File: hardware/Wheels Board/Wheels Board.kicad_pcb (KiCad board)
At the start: 2 copper layers, 45 parts, among them J1 53307-2471, J2 MX150_02x04_Vertical, J4 Conn_01x08_Socket, U1 XIAO-ESP32-S3-SMD, U2 ASM330LHHTR, U4 TPS5405DR, U5 TLV9002QDRQ1

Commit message: added uart to sch
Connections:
- J1 pad 17: /IMU_SPI_CLK -> /IMU_SPI_MOSI
- J1 pad 4: /IMU_SPI_CLK -> /ESP_UART_RX
- J1 pad 6: /IMU_SPI_CLK -> /ESP_UART_TX
- J4 pad 7: /IMU_SPI_CLK -> /IMU_SPI_MOSI
- U1 pad 3: unconnected-(U1-GPIO3_A2_D2-Pad3) -> /XIAO_HEARTBEAT_LED
- U1 pad 7: /XIAO_HEARTBEAT_LED -> /ESP_UART_TX
- U1 pad 8: unconnected-(U1-GPIO44_D7_RX-Pad8) -> /ESP_UART_RX
- U2 pad 14: /IMU_SPI_CLK -> /IMU_SPI_MOSI
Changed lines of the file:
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@@
 	(net 53 "unconnected-(U1-GPIO5_A4_D4_SDA-Pad5)")
 	(net 54 "unconnected-(U1-MTCK-Pad22)")
-	(net 55 "unconnected-(U1-GPIO3_A2_D2-Pad3)")
+	(net 55 "/ESP_UART_TX")
 	(net 56 "unconnected-(U1-MTMS-Pad21)")
 	(net 57 "unconnected-(U1-MTDO-Pad18)")
@@
 	(net 62 "unconnected-(U1-3V3-Pad12)")
 	(net 63 "unconnected-(U1-GPIO6_A5_D5_SCL-Pad6)")
-	(net 64 "unconnected-(U1-GPIO44_D7_RX-Pad8)")
+	(net 64 "/ESP_UART_RX")
 	(net 65 "unconnected-(U2-NC-Pad10)")
 	(net 66 "unconnected-(U2-NC-Pad11)")
@@
 	(net 69 "unconnected-(U5-IN2--Pad3)")
 	(net 70 "/HALL_FEEDBACK")
+	(net 71 "/IMU_SPI_MOSI")
 	(footprint "ASM330LHHTR-IMU:LGA-14L_2P5X3X0P83_STM"
 		(layer "F.Cu")
@@
 			(size 0.351536 0.57658)
 			(layers "F.Cu" "F.Mask" "F.Paste")
-			(net 19 "/IMU_SPI_CLK")
+			(net 71 "/IMU_SPI_MOSI")
 			(pinfunction "SDA")
 			(pintype "input")
@@
 			(size 0.55 1.8)
 			(layers "F.Cu" "F.Mask" "F.Paste")
-			(net 19 "/IMU_SPI_CLK")
+			(net 64 "/ESP_UART_RX")
 			(pinfunction "I2C1_SDA")
 			(pintype "bidirectional")
@@
 			(size 0.55 1.8)
 			(layers "F.Cu" "F.Mask" "F.Paste")
-			(net 19 "/IMU_SPI_CLK")
+			(net 55 "/ESP_UART_TX")
 			(pinfunction "I2C1_SCL")
 			(pintype "output")
@@
 			(size 0.55 1.8)
 			(layers "F.Cu" "F.Mask" "F.Paste")
-			(net 19 "/IMU_SPI_CLK")
+			(net 71 "/IMU_SPI_MOSI")
 			(pinfunction "SPI1_MOSI")
 			(pintype "output")
@@
 			(layers "*.Cu" "*.Mask")
 			(remove_unused_layers no)
-			(net 19 "/IMU_SPI_CLK")
+			(net 71 "/IMU_SPI_MOSI")
 			(pinfunction "Pin_7")
 			(pintype "passive")
@@
 			(layers "F.Cu" "F.Mask" "F.Paste")
 			(roundrect_rratio 0.25)
-			(net 55 "unconnected-(U1-GPIO3_A2_D2-Pad3)")
+			(net 15 "/XIAO_HEARTBEAT_LED")
 			(pinfunction "GPIO3_A2_D2")
-			(pintype "passive+no_connect")
+			(pintype "passive")
 			(solder_mask_margin 0.0508)
 			(thermal_bridge_angle 45)
@@
 			(layers "F.Cu" "F.Mask" "F.Paste")
 			(roundrect_rratio 0.25)
-			(net 15 "/XIAO_HEARTBEAT_LED")
+			(net 55 "/ESP_UART_TX")
 			(pinfunction "GPIO43_A6_D6_TX")
 			(pintype "passive")
@@
 			(layers "F.Cu" "F.Mask" "F.Paste")
 			(roundrect_rratio 0.25)
-			(net 64 "unconnected-(U1-GPIO44_D7_RX-Pad8)")
+			(net 64 "/ESP_UART_RX")
 			(pinfunction "GPIO44_D7_RX")
-			(pintype "passive+no_connect")
+			(pintype "passive")
 			(solder_mask_margin 0.0508)
 			(thermal_bridge_angle 45)

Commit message: concepts of revA layout
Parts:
- removed J2: MX150_02x04_Vertical, UTSVT_Connectors:CONN_SD-75757-002_2X04_F16p09_MOL
- removed R10, R11: 10k, Resistor_SMD:R_0603_1608Metric_Pad0.98x0.95mm_HandSolder
- removed R12, R13: 0, Resistor_SMD:R_0603_1608Metric_Pad0.98x0.95mm_HandSolder
- added J3: Conn_02x04_Counter_Clockwise, Connector_PinHeader_2.54mm:PinHeader_2x04_P2.54mm_Vertical, F.Cu at (130.5, 107.6)
- J4: value Conn_01x08_Socket -> 757571121; footprint Connector_PinHeader_2.54mm:PinHeader_1x08_P2.54mm_Vertical -> mx150_2x2:CONN_SD-75757-002_2X02_F11p20_MOL; moved to B.Cu
- TP_3.3, TP_5V1, TP_GND1: moved to B.Cu
- moved U2 49.1 mm to (128.8, 71.8)
- moved TP_5V1 48.8 mm to (89.2, 69.8), turned to 180 degrees
- moved HALL_PWR1 48.3 mm to (80.8, 107.8)
- moved TP_3.3 48.1 mm to (89.2, 66.8), turned to 180 degrees
- moved C2 47.4 mm to (131.4, 68.4), turned to 90 degrees
- moved TP_GND1 46.6 mm to (89.2, 63.8), turned to 180 degrees
- moved C3 44.7 mm to (125.4, 71.6), turned to 90 degrees
- moved C1 41.8 mm to (128.6, 68.8), turned to 180 degrees
- moved HALL_OUT1 41.6 mm to (87.0, 107.8)
- moved D2 40.6 mm to (80.6, 85.6), turned to 180 degrees
- moved D1 38.5 mm to (80.6, 84.0), turned to 180 degrees
- moved L2 37.9 mm to (120.0, 104.4)
- moved HALL_GND1 37.4 mm to (92.0, 108.0)
- moved D3 36.8 mm to (80.6, 82.4), turned to 180 degrees
- moved D4 30.5 mm to (80.6, 87.1), turned to 180 degrees
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- renumbered TP_GND2 to HALL_GND1, TP_OUT1 to HALL_OUT1, TP_5V2 to HALL_PWR1
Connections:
- J4 pad 1: /ESP_SPI_SS -> +24V
- J4 pad 2: /ESP_SPI_CLK -> /CAN_H
- J4 pad 3: /ESP_SPI_MOSI -> /CAN_L
- J4 pad 4: /ESP_SPI_MISO -> GND
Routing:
- net +3.3V: track 0.00 -> 122.2 mm, vias 0 -> 10
- net +5V: track 0.00 -> 115.5 mm, vias 0 -> 4
- net +24V: track 0.00 -> 83.4 mm, vias 0 -> 5
- net /ESP_SPI_CLK: track 0.00 -> 78.1 mm, vias 0 -> 4
- net /HALL_OUT: track 0.00 -> 75.1 mm, vias 0 -> 6
- net /ESP_SPI_MOSI: track 0.00 -> 70.7 mm, vias 0 -> 4
- net /ESP_SPI_MISO: track 0.00 -> 70.7 mm, vias 0 -> 3
- net Net-(D6-K): track 0.00 -> 69.4 mm, vias 0 -> 2
- net /ESP_SPI_SS: track 0.00 -> 54.2 mm, vias 0 -> 3
- net /IMU_SPI_MOSI: track 0.00 -> 44.4 mm, vias 0 -> 4
- net /IMU_SPI_MISO: track 0.00 -> 43.1 mm, vias 0 -> 2
- net /IMU_SPI_CLK: track 0.00 -> 42.6 mm, vias 0 -> 5
- net /ESP_UART_RX: track 0.00 -> 39.4 mm
- net /XIAO_HEARTBEAT_LED: track 0.00 -> 39.0 mm, vias 0 -> 2
- net /EXTRA_GPIO1: track 0.00 -> 38.1 mm, vias 0 -> 6
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- added copper zone on F.Cu, net GND
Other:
- board outline added: 53.7 x 50.4 mm

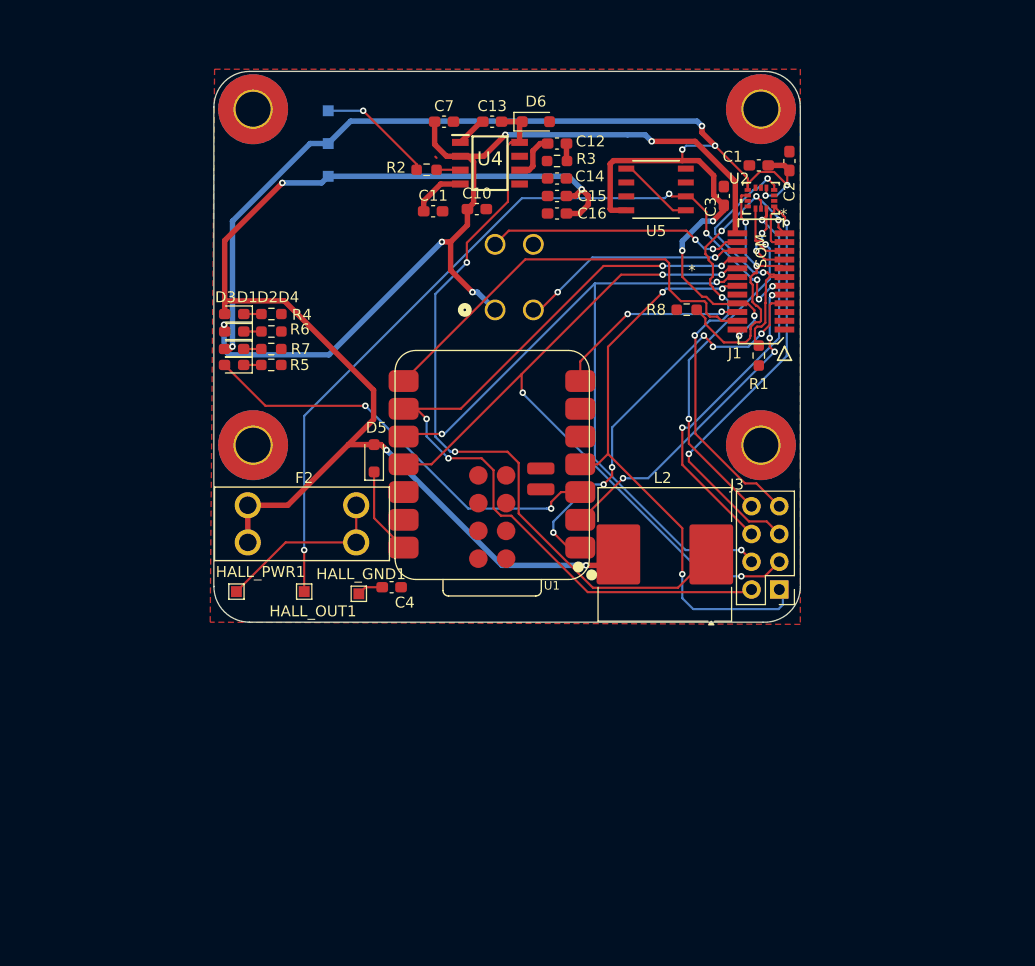
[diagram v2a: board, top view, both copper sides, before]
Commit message: review council changes, layout not finalized
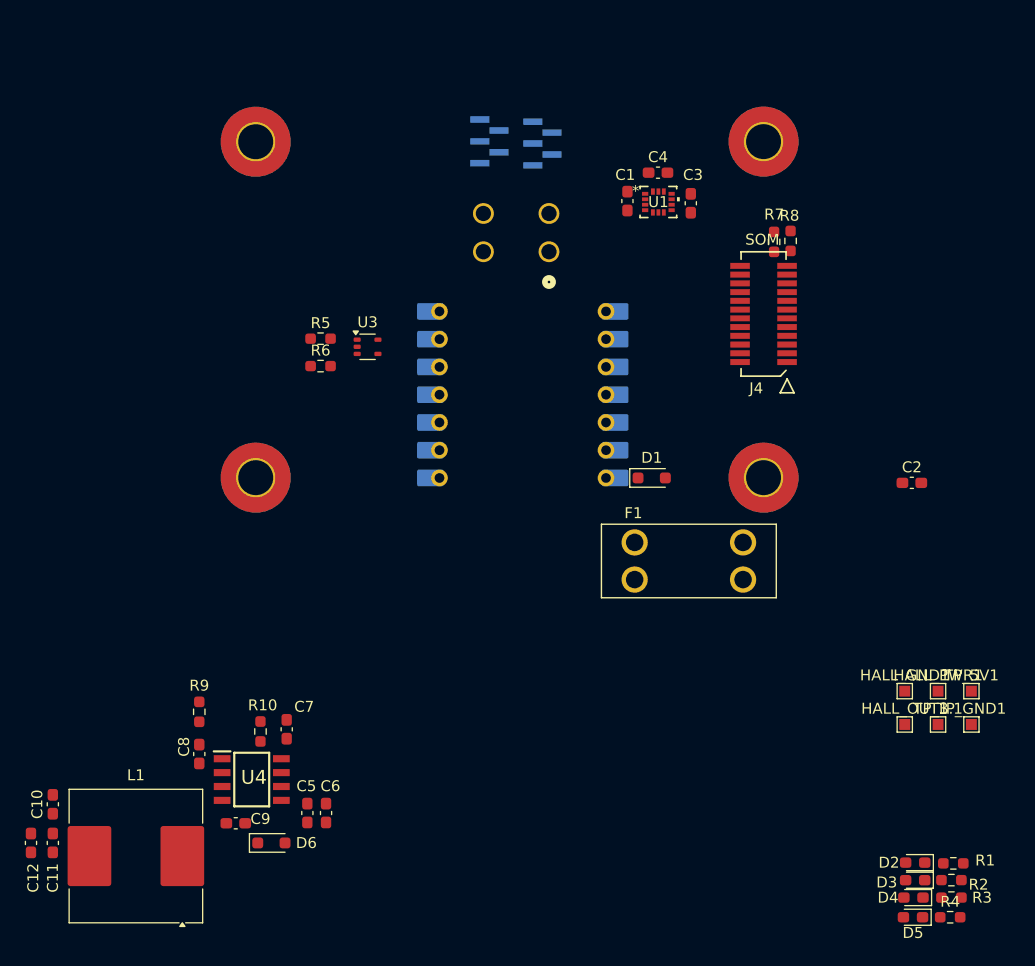
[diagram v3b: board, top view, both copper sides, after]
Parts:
- removed C13: 0.1uF, Capacitor_SMD:C_0603_1608Metric_Pad1.08x0.95mm_HandSolder
- removed C14, C15, C16: 10uF, Capacitor_SMD:C_0603_1608Metric_Pad1.08x0.95mm_HandSolder
- removed F2: Fuse, Fuse:FUSE_3568
- removed L2: 100uH, Inductor_SMD:L_Coilcraft_MSS1246-XXX
- removed TP_3.3: TestPoint, TestPoint:TestPoint_Pad_1.0x1.0mm
- removed U5: TLV9002QDRQ1, TLV9002QDRQ1:SOIC8_D_TEX
- added C5: 10uF, Capacitor_SMD:C_0603_1608Metric_Pad1.08x0.95mm_HandSolder, F.Cu at (87.3, 128.1)
- added C6: 1uF, Capacitor_SMD:C_0603_1608Metric_Pad1.08x0.95mm_HandSolder, F.Cu at (89.0, 128.1)
- added C8: 3.3nF, Capacitor_SMD:C_0603_1608Metric_Pad1.08x0.95mm_HandSolder, F.Cu at (77.4, 122.7)
- added C9: 0.1uF, Capacitor_SMD:C_0603_1608Metric_Pad1.08x0.95mm_HandSolder, F.Cu at (80.7, 129.0)
- added F1: Fuse, Fuse:FUSE_3568, F.Cu at (122.2, 105.0)
- added J2: Conn_01x05, Connector_PinHeader_1.00mm:PinHeader_1x05_P1.00mm_Vertical_SMD_Pin1Left, B.Cu at (108.8, 66.8)
- added L1: 100uH, Inductor_SMD:L_Coilcraft_MSS1246-XXX, F.Cu at (71.6, 132.0)
- added R10: ROSC, Resistor_SMD:R_0603_1608Metric_Pad0.98x0.95mm_HandSolder, F.Cu at (83.0, 120.6)
- added R9: 16k, Resistor_SMD:R_0603_1608Metric_Pad0.98x0.95mm_HandSolder, F.Cu at (77.4, 118.8)
- added TP_3.1: TestPoint, TestPoint:TestPoint_Pad_1.0x1.0mm, F.Cu at (145.0, 120.0)
- added U3: TLV9001IDCK, Package_TO_SOT_SMD:SOT-353_SC-70-5, F.Cu at (92.8, 85.4)
- C1: value 10uf -> 100nf
- C10: value 1uF -> 10uF
- C11: value 10nF -> 10uF
- C12: value 3.3nF -> 10uF
- C3: value 100nf -> 10uf
- C7: value 10uF -> 10nF
- D1: value LED -> MBR0520; footprint LED_SMD:LED_0603_1608Metric_Pad1.05x0.95mm_HandSolder -> Diode_SMD:D_SOD-323_HandSoldering
- D5: value MBR0520 -> LED; footprint Diode_SMD:D_SOD-323_HandSoldering -> LED_SMD:LED_0603_1608Metric_Pad1.05x0.95mm_HandSolder
- J1: value 53307-2471 -> Conn_01x05; footprint UTSVT_Connectors:PeripheralSOM -> Connector_PinHeader_1.00mm:PinHeader_1x05_P1.00mm_Vertical_SMD_Pin1Left; moved to B.Cu
- J3: value Conn_02x04_Counter_Clockwise -> Conn_01x04; footprint Connector_PinHeader_2.54mm:PinHeader_2x04_P2.54mm_Vertical -> mx150_2x2:CONN_SD-75757-002_2X02_F11p20_MOL; moved to B.Cu
- J4: value 757571121 -> 53307-2471; footprint mx150_2x2:CONN_SD-75757-002_2X02_F11p20_MOL -> UTSVT_Connectors:PeripheralSOM; moved to F.Cu
- R1: value 10k -> 1.5k
- R2: value ROSC -> 1.5k
- R3: value 16k -> 1.5k
- R5, R7: value 1.5k -> 10k
- R6: value 1.5k -> 19k
- TP_5V1, TP_GND1: moved to F.Cu
- U1: value XIAO-ESP32-S3-SMD -> ASM330LHHTR; footprint XIAO-ESP32S3-SMD:XIAO-ESP32S3-SMD -> ASM330LHHTR-IMU:LGA-14L_2P5X3X0P83_STM
- U2: value ASM330LHHTR -> XIAO-ESP32-S3-SMD; footprint ASM330LHHTR-IMU:LGA-14L_2P5X3X0P83_STM -> XIAO-ESP32S3:XIAO-ESP32S3-DIP; moved to B.Cu
- moved R4 83.1 mm to (146.1, 137.6)
- moved TP_GND1 81.3 mm to (148.1, 120.0), turned to 0 degrees
- moved D3 81.0 mm to (142.9, 134.2)
- moved R2 80.8 mm to (146.2, 134.2), turned to 0 degrees
- moved C12 80.1 mm to (62.0, 130.8), turned to 90 degrees
- moved D4 79.0 mm to (142.8, 135.8)
- moved D2 78.1 mm to (142.9, 132.6)
- moved R3 76.5 mm to (146.2, 135.8), turned to 0 degrees
- moved TP_5V1 75.4 mm to (148.1, 116.9), turned to 0 degrees
- moved D6 70.3 mm to (84.0, 130.8)
- moved C11 67.5 mm to (64.0, 130.8), turned to 90 degrees
- moved C10 66.9 mm to (64.0, 127.3), turned to 90 degrees
- moved HALL_PWR1 64.8 mm to (145.0, 116.9)
- moved D5 64.8 mm to (142.7, 137.6), turned to 180 degrees
- moved U4 60.5 mm to (82.2, 125.0)
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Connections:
- C10 pad 1: +24V -> +5V
- C11 pad 1: Net-(U4-SS) -> +5V
- C12 pad 1: Net-(U4-COMP) -> +5V
- C12 pad 2: Net-(C12-Pad2) -> GND
- C2 pad 1: +3.3V -> Net-(C2-Pad1)
- C4 pad 1: Net-(C4-Pad1) -> +3.3V
- C7 pad 1: +24V -> Net-(U4-SS)
- D1 pad 2: +24V -> +5V
- D2 pad 2: +3.3V -> +5V
- D3 pad 2: +5V -> +24V
- D4 pad 2: /XIAO_HEARTBEAT_LED -> +3.3V
- D5 pad 2: +5V -> /XIAO_HEARTBEAT_LED
- HALL_GND1 pad 1: Net-(C4-Pad1) -> GND
- HALL_PWR1 pad 1: Net-(F2-Pad2) -> Net-(C2-Pad1)
- J1 pad 1: GND -> /ESP_SPI_SS
- J1 pad 2: +3.3V -> /ESP_SPI_CLK
- J1 pad 3: GND -> /ESP_SPI_MOSI
- J1 pad 4: /ESP_UART_RX -> /ESP_SPI_MISO
- J3 pad 1: /ESP_SPI_SS -> +24V
- J3 pad 2: /ESP_SPI_CLK -> /CAN_H
- J3 pad 3: /ESP_SPI_MOSI -> /CAN_L
- J3 pad 4: /ESP_SPI_MISO -> GND
- J4 pad 1: +24V -> GND
- J4 pad 2: /CAN_H -> +3.3V
- J4 pad 3: /CAN_L -> GND
- J4 pad 4: GND -> /ESP_UART_RX
- R1 pad 1: /IMU_INT1 -> Net-(D2-K)
- R2 pad 1: /24v to 5v convertor/ROSC -> Net-(D3-K)
- R3 pad 1: Net-(C12-Pad2) -> Net-(D4-K)
- R4 pad 1: Net-(D3-K) -> Net-(D5-K)
- R5 pad 1: Net-(D4-K) -> /HALL_OUT
- R5 pad 2: GND -> Net-(U3-+)
- R6 pad 1: Net-(D1-K) -> GND
- R6 pad 2: GND -> Net-(U3-+)
- R7 pad 1: Net-(D2-K) -> /IMU_INT2
- R8 pad 1: /IMU_INT2 -> /IMU_INT1
- U1 pad 1: /EXTRA_GPIO1 -> /IMU_SPI_MISO
- U1 pad 10: /ESP_SPI_MISO -> unconnected-(U1-NC-Pad10)
- U1 pad 11: /ESP_SPI_MOSI -> unconnected-(U1-NC-Pad11)
- U1 pad 12: unconnected-(U1-3V3-Pad12) -> /IMU_SPI_SS
- U1 pad 13: GND -> /IMU_SPI_CLK
- U1 pad 14: Net-(D5-K) -> /IMU_SPI_MOSI
- U1 pad 2: /EXTRA_GPIO2 -> GND
- U1 pad 3: /XIAO_HEARTBEAT_LED -> GND
- U1 pad 4: /ESP_SPI_SS -> /IMU_INT1
- U1 pad 5: unconnected-(U1-GPIO5_A4_D4_SDA-Pad5) -> +3.3V
- U1 pad 6: unconnected-(U1-GPIO6_A5_D5_SCL-Pad6) -> GND
- U1 pad 7: /ESP_UART_TX -> GND
- U1 pad 8: /ESP_UART_RX -> +3.3V
- U1 pad 9: /ESP_SPI_CLK -> /IMU_INT2
- U2 pad 1: /IMU_SPI_MISO -> /EXTRA_GPIO1
- U2 pad 10: unconnected-(U2-NC-Pad10) -> /ESP_SPI_MISO
- U2 pad 11: unconnected-(U2-NC-Pad11) -> /ESP_SPI_MOSI
- U2 pad 12: /IMU_SPI_SS -> unconnected-(U2-3V3-Pad12)_1
- U2 pad 13: /IMU_SPI_CLK -> GND
- U2 pad 14: /IMU_SPI_MOSI -> Net-(D1-K)
- U2 pad 2: GND -> /EXTRA_GPIO2
- U2 pad 3: GND -> /XIAO_HEARTBEAT_LED
- U2 pad 4: /IMU_INT1 -> /ESP_SPI_SS
- U2 pad 5: +3.3V -> unconnected-(U2-GPIO5_A4_D4_SDA-Pad5)_1
- U2 pad 6: GND -> unconnected-(U2-GPIO6_A5_D5_SCL-Pad6)
- U2 pad 7: GND -> /ESP_UART_TX
- U2 pad 8: +3.3V -> /ESP_UART_RX
- U2 pad 9: /IMU_INT2 -> /ESP_SPI_CLK
- U4 pad 5: +5V_BUCK -> +5V
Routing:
- net +3.3V: track 122.2 -> 0.00 mm, vias 10 -> 0
- net +5V: track 115.5 -> 0.00 mm, vias 4 -> 0
- net +24V: track 83.4 -> 0.00 mm, vias 5 -> 0
- net /ESP_SPI_CLK: track 78.1 -> 0.00 mm, vias 4 -> 0
- net /HALL_OUT: track 75.1 -> 0.00 mm, vias 6 -> 0
- net /ESP_SPI_MOSI: track 70.7 -> 0.00 mm, vias 4 -> 0
- net /ESP_SPI_MISO: track 70.7 -> 0.00 mm, vias 3 -> 0
- net Net-(D6-K): track 69.4 -> 0.00 mm, vias 2 -> 0
- net /ESP_SPI_SS: track 54.2 -> 0.00 mm, vias 3 -> 0
- net /IMU_SPI_MOSI: track 44.4 -> 0.00 mm, vias 4 -> 0
- net /IMU_SPI_MISO: track 43.1 -> 0.00 mm, vias 2 -> 0
- net /IMU_SPI_CLK: track 42.6 -> 0.00 mm, vias 5 -> 0
- net /ESP_UART_RX: track 39.4 -> 0.00 mm
- net /XIAO_HEARTBEAT_LED: track 39.0 -> 0.00 mm, vias 2 -> 0
- net /EXTRA_GPIO1: track 38.1 -> 0.00 mm, vias 6 -> 0
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- removed copper zone on F.Cu, net GND
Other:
- board outline removed

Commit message: pre wiring layout
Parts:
- HALL_GND1, HALL_OUT1, HALL_PWR1: footprint TestPoint:TestPoint_Pad_1.0x1.0mm -> Connector_PinHeader_2.54mm:PinHeader_1x01_P2.54mm_Vertical
- J1, J2: footprint Connector_PinHeader_1.00mm:PinHeader_1x05_P1.00mm_Vertical_SMD_Pin1Left -> Connector_PinHeader_1.00mm:PinHeader_1x05_P1.00mm_Vertical
- TP_3.1, TP_5V1, TP_GND1: moved to B.Cu
- moved TP_GND1 49.1 mm to (121.0, 78.9)
- moved TP_3.1 49.1 mm to (118.0, 78.9)
- moved R1 47.1 mm to (104.5, 111.1)
- moved D3 47.1 mm to (101.0, 112.6)
- moved D2 47.1 mm to (101.0, 111.0)
- moved R2 47.1 mm to (104.3, 112.6)
- moved TP_5V1 44.2 mm to (121.0, 82.0)
- moved D4 39.6 mm to (112.2, 110.6)
- moved R3 39.6 mm to (115.6, 110.6)
- moved D5 39.6 mm to (112.1, 112.4)
- moved R4 39.6 mm to (115.5, 112.4)
- moved R5 38.1 mm to (126.2, 90.6), turned to 180 degrees
- moved R6 38.1 mm to (126.2, 93.1)
- moved U3 37.4 mm to (129.6, 91.8)
- moved D6 33.5 mm to (96.8, 99.8)
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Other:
- board outline added: 53.6 x 50.5 mm

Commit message: revised layout again
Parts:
- removed J3: Conn_01x04, mx150_2x2:CONN_SD-75757-002_2X02_F11p20_MOL
- added J5: MX150_02x02_Vertical, UTSVT_Connectors:MX150_02x02_Vertical, B.Cu at (108.8, 83.0)
- U2: moved to F.Cu
- moved TP_5V1 22.9 mm to (104.4, 66.2)
- moved U2 21.8 mm to (106.6, 95.4)
- moved D1 21.3 mm to (99.8, 107.0)
- moved TP_GND1 19.3 mm to (106.6, 66.2)
- moved TP_3.1 15.8 mm to (108.8, 66.0)
- moved J2 15.4 mm to (122.6, 73.6), turned to 180 degrees
- moved F1 13.9 mm to (120.2, 110.0)
- moved R8 13.1 mm to (129.0, 88.6), turned to -90 degrees
- moved C5 12.5 mm to (90.3, 89.1)
- moved C6 12.5 mm to (92.0, 89.1)
- moved D5 12.5 mm to (118.4, 101.6)
- moved R4 12.5 mm to (121.8, 101.6)
- moved HALL_PWR1 12.4 mm to (130.4, 110.2)
- moved R9 12.3 mm to (93.0, 99.8), turned to 0 degrees
- moved C7 11.3 mm to (86.8, 89.2)
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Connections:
- U3 pad 1: Net-(U3-+) -> /HALL_OUT
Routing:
- net /IMU_INT1: track 0.00 -> 17.6 mm, vias 0 -> 2
- net /IMU_INT2: track 0.00 -> 15.7 mm
- net /IMU_SPI_MOSI: track 0.00 -> 6.55 mm, vias 0 -> 2
- net /IMU_SPI_SS: track 0.00 -> 4.80 mm
- net /IMU_SPI_MISO: track 0.00 -> 4.50 mm, vias 0 -> 2
- net /HALL_OUT: track 0.00 -> 4.25 mm
- net /IMU_SPI_CLK: track 0.00 -> 2.91 mm
- net /HALL_FEEDBACK: track 0.00 -> 1.90 mm

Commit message: revised layout
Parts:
- removed R5: 10k, Resistor_SMD:R_0603_1608Metric_Pad0.98x0.95mm_HandSolder
- removed R6: 19k, Resistor_SMD:R_0603_1608Metric_Pad0.98x0.95mm_HandSolder
- added REF**: PinHeader_1x01_P2.00mm_Vertical, Connector_PinHeader_2.00mm:PinHeader_1x01_P2.00mm_Vertical, F.Cu at (98.4, 61.4)
- added REF**: PinHeader_1x01_P2.00mm_Vertical, Connector_PinHeader_2.00mm:PinHeader_1x01_P2.00mm_Vertical, F.Cu at (98.5, 70.0)
- moved U2 29.1 mm to (97.3, 67.8), turned to 0 degrees
- moved D1 29.1 mm to (90.4, 79.5), turned to 180 degrees
- moved TP_5V1 26.1 mm to (92.0, 89.2)
- moved TP_3.1 26.1 mm to (96.4, 89.0)
- moved TP_GND1 26.1 mm to (94.2, 89.2)
- moved R8 24.9 mm to (117.4, 66.6), turned to 180 degrees
- moved C6 22.1 mm to (102.9, 108.4), turned to 0 degrees
- moved C7 21.7 mm to (103.0, 103.7), turned to 0 degrees
- moved C5 21.7 mm to (102.9, 106.8), turned to 0 degrees
- moved R10 21.6 mm to (102.9, 105.2), turned to 0 degrees
- moved R4 16.7 mm to (105.9, 106.8), turned to -90 degrees
- moved C1 15.7 mm to (115.6, 68.4), turned to 180 degrees
- moved R7 15.5 mm to (120.8, 72.0), turned to 0 degrees
- moved D6 15.3 mm to (95.9, 111.4), turned to 0 degrees
- moved U4 13.8 mm to (97.5, 106.0), turned to 180 degrees
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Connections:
- J1 pad 2: /ESP_SPI_CLK -> /ESP_SPI_MISO
- J1 pad 4: /ESP_SPI_MISO -> /ESP_SPI_CLK
- J2 pad 1: /IMU_SPI_SS -> /IMU_SPI_CLK
- J2 pad 2: /IMU_SPI_CLK -> /IMU_SPI_MISO
- J2 pad 3: /IMU_SPI_MOSI -> /IMU_SPI_SS
- J2 pad 4: /IMU_SPI_MISO -> /IMU_SPI_MOSI
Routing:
- net +3.3V: track 0.00 -> 91.2 mm, vias 0 -> 3
- net +5V: track 0.00 -> 63.9 mm, vias 0 -> 1
- net /EXTRA_GPIO1: track 0.00 -> 54.7 mm, vias 0 -> 4
- net +24V: track 0.00 -> 53.3 mm, vias 0 -> 7
- net /EXTRA_GPIO2: track 0.00 -> 52.0 mm, vias 0 -> 2
- net /XIAO_HEARTBEAT_LED: track 0.00 -> 50.0 mm, vias 0 -> 4
- net /ESP_SPI_SS: track 0.00 -> 47.0 mm
- net /ESP_UART_TX: track 0.00 -> 42.3 mm, vias 0 -> 2
- net /ESP_SPI_MOSI: track 0.00 -> 29.3 mm, vias 0 -> 2
- net /CAN_L: track 0.00 -> 28.9 mm, vias 0 -> 4
- net /ESP_SPI_MISO: track 0.00 -> 27.9 mm, vias 0 -> 2
- net /ESP_UART_RX: track 0.00 -> 27.1 mm, vias 0 -> 2
- net Net-(D1-K): track 0.00 -> 26.8 mm, vias 0 -> 4
- net /ESP_SPI_CLK: track 0.00 -> 24.3 mm, vias 0 -> 2
- net /CAN_H: track 0.00 -> 22.8 mm, vias 0 -> 4
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- added copper zone on B.Cu, net GND
- added copper zone on F.Cu, net GND
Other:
- board size 53.6 x 50.5 mm -> 53.6 x 57.1 mm
- board text added: "SOM"
